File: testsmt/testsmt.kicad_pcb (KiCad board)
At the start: 2 copper layers, 100 x 100 mm, 47 parts, among them J1 DIN-5_180degree, J2 Conn_01x16, J3 Conn_01x16, J4 Conn_01x16, J5 AudioJack3_Ground_Switch, U1 6N138, U2 Teensy3.2, U3 4051, U4 4051, U5 4051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

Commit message: where is the last unrouted connection?!
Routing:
- net /DAC_OUTPUT: track 0.00 -> 99.1 mm, vias 0 -> 1
- net +5V: track 4.66 -> 94.6 mm, vias 0 -> 1
- net Net-(C2-Pad2): track 13.4 -> 96.1 mm, vias 0 -> 1
- net /KNOB_READ: track 0.00 -> 75.6 mm, vias 0 -> 1
- net +3V3: track 423.3 -> 477.0 mm, vias 5 -> 6
- net /LDR: track 0.00 -> 17.1 mm
- net GND: track 6.65 -> 18.6 mm, vias 4 -> 6
- net Net-(C2-Pad1): track 0.00 -> 11.5 mm
- net Net-(R1-Pad2): track 0.00 -> 9.89 mm
- net Net-(D1-Pad2): track 0.00 -> 3.12 mm
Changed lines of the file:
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@@
     (thickness 1.6)
     (drawings 15)
-    (tracks 815)
+    (tracks 886)
     (zones 0)
     (modules 47)
@@
   (segment (start 49.155 52.445) (end 49 52.6) (width 0.25) (layer F.Cu) (net 1))
   (via (at 50.3 39.9) (size 0.8) (drill 0.4) (layers F.Cu B.Cu) (net 1))
-  (via (at 139.1 32.284999) (size 0.8) (drill 0.4) (layers F.Cu B.Cu) (net 1))
   (segment (start 140.7 32.365) (end 139.180001 32.365) (width 0.25) (layer F.Cu) (net 1))
   (segment (start 139.180001 32.365) (end 139.1 32.284999) (width 0.25) (layer F.Cu) (net 1))
+  (via (at 139.1 32.284999) (size 0.8) (drill 0.4) (layers F.Cu B.Cu) (net 1))
+  (via (at 135.000011 38.4) (size 0.8) (drill 0.4) (layers F.Cu B.Cu) (net 1))
+  (segment (start 139.1 32.284999) (end 139.1 34.300011) (width 0.25) (layer B.Cu) (net 1))
+  (segment (start 139.1 34.300011) (end 135.000011 38.4) (width 0.25) (layer B.Cu) (net 1))
+  (segment (start 135.000011 37.744989) (end 135.3 37.445) (width 0.25) (layer F.Cu) (net 1))
+  (segment (start 135.000011 38.4) (end 135.000011 37.744989) (width 0.25) (layer F.Cu) (net 1))
+  (via (at 74.1 103.1) (size 0.8) (drill 0.4) (layers F.Cu B.Cu) (net 1))
+  (segment (start 74.1 102.925) (end 74.1 103.1) (width 0.25) (layer F.Cu) (net 1))
+  (segment (start 76.3 101.175) (end 75.85 101.175) (width 0.25) (layer F.Cu) (net 1))
+  (segment (start 75.85 101.175) (end 74.1 102.925) (width 0.25) (layer F.Cu) (net 1))
+  (via (at 94.6 98.7) (size 0.8) (drill 0.4) (layers F.Cu B.Cu) (net 3))
+  (segment (start 94.4 98.5) (end 94.6 98.7) (width 0.25) (layer F.Cu) (net 3))
+  (segment (start 125.08 62.51) (end 94.4 93.19) (width 0.25) (layer F.Cu) (net 3))
+  (segment (start 94.4 93.19) (end 94.4 98.5) (width 0.25) (layer F.Cu) (net 3))
+  (segment (start 50.899999 100.899999) (end 50 100) (width 0.25) (layer B.Cu) (net 3))
+  (segment (start 56.025001 106.025001) (end 50.899999 100.899999) (width 0.25) (layer B.Cu) (net 3))
+  (segment (start 87.274999 106.025001) (end 56.025001 106.025001) (width 0.25) (layer B.Cu) (net 3))
+  (segment (start 94.6 98.7) (end 87.274999 106.025001) (width 0.25) (layer B.Cu) (net 3))
   (via (at 46.3 60.3) (size 0.8) (drill 0.4) (layers F.Cu B.Cu) (net 5))
   (segment (start 46.3 71.730002) (end 46.3 60.3) (width 0.25) (layer F.Cu) (net 5))
@@
   (segment (start 117.46 63.64137) (end 108.54637 72.555) (width 0.25) (layer F.Cu) (net 5))
   (segment (start 117.46 62.51) (end 117.46 63.64137) (width 0.25) (layer F.Cu) (net 5))
-  (segment (start 56.7 72.555) (end 91 72.555) (width 0.25) (layer F.Cu) (net 5))
   (segment (start 91 72.555) (end 91.415 72.555) (width 0.25) (layer F.Cu) (net 5))
   (segment (start 117.46 61.37863) (end 117 60.91863) (width 0.25) (layer B.Cu) (net 5))
@@
   (segment (start 116.634315 26.8) (end 115.069316 28.364999) (width 0.25) (layer B.Cu) (net 5))
   (segment (start 117.2 26.8) (end 116.634315 26.8) (width 0.25) (layer B.Cu) (net 5))
+  (via (at 87.9 74.3) (size 0.8) (drill 0.4) (layers F.Cu B.Cu) (net 5))
+  (segment (start 80 84) (end 80 82.2) (width 0.25) (layer B.Cu) (net 5))
+  (segment (start 80 82.2) (end 87.9 74.3) (width 0.25) (layer B.Cu) (net 5))
+  (segment (start 89.645 72.555) (end 89.8 72.555) (width 0.25) (layer F.Cu) (net 5))
+  (segment (start 87.9 74.3) (end 89.645 72.555) (width 0.25) (layer F.Cu) (net 5))
+  (segment (start 56.7 72.555) (end 89.8 72.555) (width 0.25) (layer F.Cu) (net 5))
+  (segment (start 89.8 72.555) (end 91 72.555) (width 0.25) (layer F.Cu) (net 5))
+  (segment (start 106 119.727208) (end 106 121) (width 0.25) (layer F.Cu) (net 5))
+  (segment (start 106 116.822588) (end 106 119.727208) (width 0.25) (layer F.Cu) (net 5))
+  (segment (start 82.732412 93.555) (end 106 116.822588) (width 0.25) (layer F.Cu) (net 5))
+  (segment (start 81.7 93.555) (end 82.732412 93.555) (width 0.25) (layer F.Cu) (net 5))
   (segment (start 50.3 46.095) (end 47.2 49.195) (width 0.25) (layer F.Cu) (net 7))
   (segment (start 51.3 46.095) (end 50.3 46.095) (width 0.25) (layer F.Cu) (net 7))
@@
   (segment (start 51.5 70.3) (end 88.4 70.3) (width 0.25) (layer F.Cu) (net 7))
   (segment (start 88.4 70.3) (end 88.59 70.3) (width 0.25) (layer F.Cu) (net 7))
+  (segment (start 123.681237 67.443763) (end 123.125 68) (width 0.25) (layer F.Cu) (net 8))
+  (segment (start 126.494999 64.630001) (end 123.681237 67.443763) (width 0.25) (layer F.Cu) (net 8))
+  (segment (start 126.494999 61.095001) (end 126.494999 64.630001) (width 0.25) (layer F.Cu) (net 8))
+  (segment (start 127.62 59.97) (end 126.494999 61.095001) (width 0.25) (layer F.Cu) (net 8))
+  (via (at 79.3 94.1) (size 0.8) (drill 0.4) (layers F.Cu B.Cu) (net 10))
+  (segment (start 78.745 94.1) (end 79.3 94.1) (width 0.25) (layer F.Cu) (net 10))
+  (segment (start 76.3 96.095) (end 76.75 96.095) (width 0.25) (layer F.Cu) (net 10))
+  (segment (start 76.75 96.095) (end 78.745 94.1) (width 0.25) (layer F.Cu) (net 10))
+  (segment (start 97.695002 94.1) (end 129.8 61.995002) (width 0.25) (layer B.Cu) (net 10))
+  (segment (start 79.3 94.1) (end 97.695002 94.1) (width 0.25) (layer B.Cu) (net 10))
+  (segment (start 129.8 57.07) (end 127.62 54.89) (width 0.25) (layer B.Cu) (net 10))
+  (segment (start 129.8 61.995002) (end 129.8 57.07) (width 0.25) (layer B.Cu) (net 10))
   (segment (start 50.3 32.095) (end 50.224999 32.019999) (width 0.25) (layer F.Cu) (net 11))
   (segment (start 51.3 32.095) (end 50.3 32.095) (width 0.25) (layer F.Cu) (net 11))
@@
   (segment (start 122.1525 96.19) (end 122.3425 96) (width 0.25) (layer F.Cu) (net 20))
   (segment (start 117.765 96.19) (end 122.1525 96.19) (width 0.25) (layer F.Cu) (net 20))
+  (via (at 118.5 71.1) (size 0.8) (drill 0.4) (layers F.Cu B.Cu) (net 20))
+  (segment (start 126.494999 63.105001) (end 118.5 71.1) (width 0.25) (layer B.Cu) (net 20))
+  (segment (start 127.62 29.49) (end 126.494999 30.615001) (width 0.25) (layer B.Cu) (net 20))
+  (segment (start 126.494999 30.615001) (end 126.494999 63.105001) (width 0.25) (layer B.Cu) (net 20))
+  (segment (start 123.927609 71.1) (end 135 82.172391) (width 0.25) (layer F.Cu) (net 20))
+  (segment (start 118.5 71.1) (end 123.927609 71.1) (width 0.25) (layer F.Cu) (net 20))
+  (segment (start 122.898737 95.443763) (end 122.3425 96) (width 0.25) (layer F.Cu) (net 20))
+  (segment (start 123.36751 94.97499) (end 122.898737 95.443763) (width 0.25) (layer F.Cu) (net 20))
+  (segment (start 130.856419 94.97499) (end 123.36751 94.97499) (width 0.25) (layer F.Cu) (net 20))
+  (segment (start 135 90.831409) (end 130.856419 94.97499) (width 0.25) (layer F.Cu) (net 20))
+  (segment (start 135 82.172391) (end 135 90.831409) (width 0.25) (layer F.Cu) (net 20))
   (segment (start 52.3 75.095) (end 53.9 73.495) (width 0.25) (layer F.Cu) (net 26))
   (segment (start 51.3 75.095) (end 52.3 75.095) (width 0.25) (layer F.Cu) (net 26))
@@
   (segment (start 135.59 106) (end 135.51499 105.92499) (width 0.25) (layer F.Cu) (net 53))
   (segment (start 137.59 106) (end 135.59 106) (width 0.25) (layer F.Cu) (net 53))
+  (via (at 69.3 107.7) (size 0.8) (drill 0.4) (layers F.Cu B.Cu) (net 53))
+  (segment (start 64.00001 102.40001) (end 69.3 107.7) (width 0.25) (layer F.Cu) (net 53))
+  (segment (start 63 97.3) (end 64.00001 98.30001) (width 0.25) (layer F.Cu) (net 53))
+  (segment (start 64.00001 98.30001) (end 64.00001 102.40001) (width 0.25) (layer F.Cu) (net 53))
+  (segment (start 137.59 107.125) (end 137.59 106) (width 0.25) (layer B.Cu) (net 53))
+  (segment (start 137.015 107.7) (end 137.59 107.125) (width 0.25) (layer B.Cu) (net 53))
+  (segment (start 69.3 107.7) (end 137.015 107.7) (width 0.25) (layer B.Cu) (net 53))
   (segment (start 129.5009 88.99618) (end 120.50382 88.99618) (width 0.25) (layer F.Cu) (net 54))
   (segment (start 120.50382 88.99618) (end 112.5 97) (width 0.25) (layer F.Cu) (net 54))
@@
   (segment (start 121.87118 79.00382) (end 129.5009 79.00382) (width 0.25) (layer F.Cu) (net 57))
   (segment (start 104.875 96) (end 121.87118 79.00382) (width 0.25) (layer F.Cu) (net 57))
+  (segment (start 125.5875 68) (end 128.125 68) (width 0.25) (layer F.Cu) (net 59))
+  (segment (start 125 68) (end 125.5875 68) (width 0.25) (layer F.Cu) (net 59))
+  (segment (start 75.85 94.825) (end 76.3 94.825) (width 0.25) (layer F.Cu) (net 60))
+  (segment (start 75.224999 94.199999) (end 75.85 94.825) (width 0.25) (layer F.Cu) (net 60))
+  (segment (start 75.224999 87.437082) (end 75.224999 94.199999) (width 0.25) (layer F.Cu) (net 60))
+  (segment (start 77.46 85.202081) (end 75.224999 87.437082) (width 0.25) (layer F.Cu) (net 60))
+  (segment (start 77.46 84) (end 77.46 85.202081) (width 0.25) (layer F.Cu) (net 60))
+  (segment (start 72.7625 94.825) (end 72 94.0625) (width 0.25) (layer F.Cu) (net 60))
+  (segment (start 76.3 94.825) (end 72.7625 94.825) (width 0.25) (layer F.Cu) (net 60))
   (segment (start 136.745 70.4775) (end 139.3625 70.4775) (width 0.25) (layer F.Cu) (net 61))
   (segment (start 136.1575 70.4775) (end 136.745 70.4775) (width 0.25) (layer F.Cu) (net 61))
@@
   (segment (start 135.1 65.58) (end 134.2825 66.3975) (width 0.25) (layer F.Cu) (net 78))
   (segment (start 135.1 65) (end 135.1 65.58) (width 0.25) (layer F.Cu) (net 78))
+  (segment (start 53.399999 100.899999) (end 52.5 100) (width 0.25) (layer F.Cu) (net 79))
+  (segment (start 53.725001 101.225001) (end 53.399999 100.899999) (width 0.25) (layer F.Cu) (net 79))
+  (segment (start 60.999999 101.225001) (end 53.725001 101.225001) (width 0.25) (layer F.Cu) (net 79))
+  (segment (start 62.225 100) (end 60.999999 101.225001) (width 0.25) (layer F.Cu) (net 79))
+  (segment (start 63 100) (end 62.225 100) (width 0.25) (layer F.Cu) (net 79))
   (segment (start 82.15 97.365) (end 81.7 97.365) (width 0.25) (layer F.Cu) (net 80))
   (segment (start 83.95001 99.16501) (end 82.15 97.365) (width 0.25) (layer F.Cu) (net 80))

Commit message: routing done
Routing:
- net Net-(U2-Pad52): track 0.00 -> 3.81 mm
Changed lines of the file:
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@@
     (thickness 1.6)
     (drawings 15)
-    (tracks 886)
+    (tracks 888)
     (zones 0)
     (modules 47)
@@
     (38 B.Mask user)
     (39 F.Mask user)
-    (40 Dwgs.User user hide)
+    (40 Dwgs.User user)
     (41 Cmts.User user)
     (42 Eco1.User user)
@@
   (segment (start 124.1 98.9) (end 122 101) (width 0.25) (layer F.Cu) (net 36))
   (segment (start 124.9 98.9) (end 124.1 98.9) (width 0.25) (layer F.Cu) (net 36))
+  (segment (start 120 38.306498) (end 120 35.84) (width 0.25) (layer F.Cu) (net 50))
+  (segment (start 120 39.65) (end 120 38.306498) (width 0.25) (layer F.Cu) (net 50))
   (segment (start 136.715 96) (end 137.59 96) (width 0.25) (layer F.Cu) (net 53))
   (segment (start 135.51499 97.20001) (end 136.715 96) (width 0.25) (layer F.Cu) (net 53))

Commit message: nearly there
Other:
- board text added: "Attack"
- board text added: "Cutoff"
- board text added: "DAC volume"
- board text added: "Decay"
- board text added: "LFO (out) Saw (out) Square (out) Filter (out) ADSR (out) VCA (out) MIDI note (out) MIDI gate (out) Saw freq (in) Square freq (in) Filter (in) Filter cutoff (in) VCA (in) VCA CV (in) ADSR gate (in) Main out (in)"
- board text added: "LFO freq"
- board text added: "Release"
- board text added: "Resonance"
- board text added: "Saw freq"
- board text added: "Sustain"
- board text added: "by Matt Bradshaw"
- board text added: "polymod mini v1"
- board text removed: "Parameter X Parameter X Parameter X Parameter X Parameter X Parameter X Parameter X Parameter X Parameter X Parameter X Parameter X Parameter X Parameter X Parameter X Parameter X Parameter X"
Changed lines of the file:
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@@
   (general
     (thickness 1.6)
-    (drawings 15)
+    (drawings 26)
     (tracks 888)
     (zones 0)
@@
       (net 50 "Net-(U2-Pad52)"))
   )
+  (gr_text "by Matt\nBradshaw" (at 59.5 85) (layer F.SilkS)
+    (effects (font (size 1.5 1.5) (thickness 0.3)) (justify left))
+  )
+  (gr_text "polymod mini v1" (at 59 79.5) (layer F.SilkS)
+    (effects (font (size 2.5 2.5) (thickness 0.5)) (justify left))
+  )
+  (gr_text "LFO freq" (at 78.5 88) (layer F.SilkS)
+    (effects (font (size 1.5 1.5) (thickness 0.3)))
+  )
+  (gr_text Cutoff (at 104 93) (layer F.SilkS)
+    (effects (font (size 1.5 1.5) (thickness 0.3)))
+  )
+  (gr_text Release (at 137.5 123) (layer F.SilkS)
+    (effects (font (size 1.5 1.5) (thickness 0.3)))
+  )
+  (gr_text Sustain (at 120.5 123) (layer F.SilkS)
+    (effects (font (size 1.5 1.5) (thickness 0.3)))
+  )
+  (gr_text Decay (at 103.5 123) (layer F.SilkS)
+    (effects (font (size 1.5 1.5) (thickness 0.3)))
+  )
+  (gr_text Attack (at 86.5 123) (layer F.SilkS)
+    (effects (font (size 1.5 1.5) (thickness 0.3)))
+  )
+  (gr_text Resonance (at 69.5 123) (layer F.SilkS)
+    (effects (font (size 1.5 1.5) (thickness 0.3)))
+  )
+  (gr_text "Saw freq" (at 52.7 123) (layer F.SilkS)
+    (effects (font (size 1.5 1.5) (thickness 0.3)))
+  )
+  (gr_text "DAC volume" (at 52.7 102.6) (layer F.SilkS)
+    (effects (font (size 1.5 1.5) (thickness 0.3)))
+  )
   (gr_line (start 99 50) (end 99 92) (layer Dwgs.User) (width 0.2))
   (gr_line (start 109 50) (end 99 50) (layer Dwgs.User) (width 0.2))
@@
   (gr_line (start 145 25) (end 145 125) (layer Edge.Cuts) (width 0.2))
   (gr_line (start 45 25) (end 145 25) (layer Edge.Cuts) (width 0.2))
-  (gr_text "Parameter X\nParameter X\nParameter X\nParameter X\nParameter X\nParameter X\nParameter X\nParameter X\nParameter X\nParameter X\nParameter X\nParameter X\nParameter X\nParameter X\nParameter X\nParameter X" (at 85.6 48) (layer F.SilkS)
-    (effects (font (size 1.5 1.5) (thickness 0.3)))
+  (gr_text "LFO (out)\nSaw (out)\nSquare (out)\nFilter (out)\nADSR (out)\nVCA (out)\nMIDI note (out)\nMIDI gate (out)\nSaw freq (in)\nSquare freq (in)\nFilter (in)\nFilter cutoff (in)\nVCA (in)\nVCA CV (in)\nADSR gate (in)\nMain out (in)" (at 78.7 48) (layer F.SilkS)
+    (effects (font (size 1.5 1.5) (thickness 0.3)) (justify left))
   )
   (via (at 49.2 65.1) (size 0.8) (drill 0.4) (layers F.Cu B.Cu) (net 1))

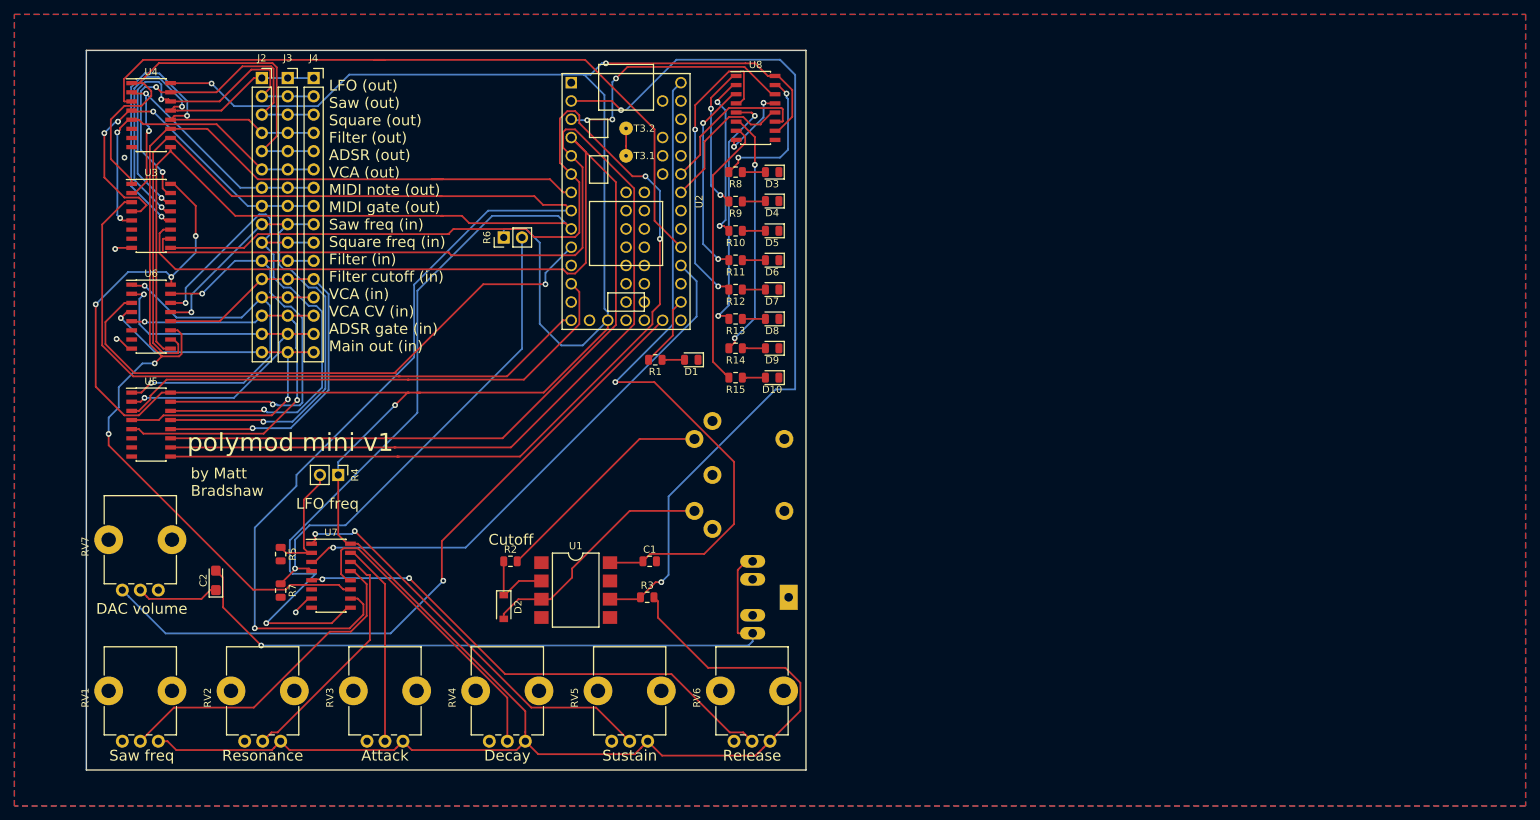
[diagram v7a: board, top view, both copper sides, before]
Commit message: mounting holes
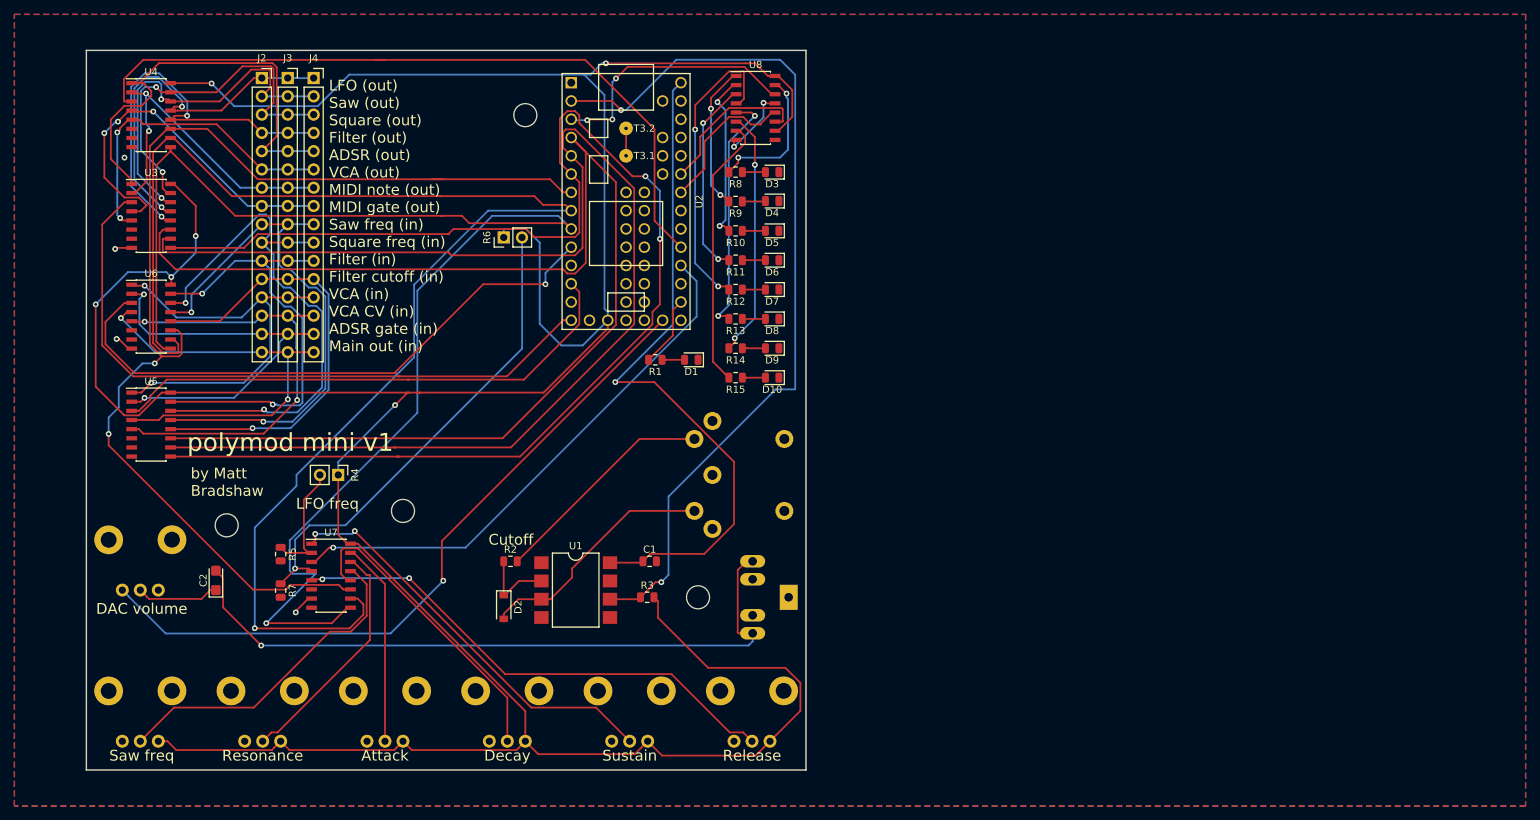
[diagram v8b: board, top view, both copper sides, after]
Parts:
- added H1: MountingHole, polymodsmt:MountingHole_3.2mm_M3, F.Cu at (64.5, 91.0)
- added H2: MountingHole, polymodsmt:MountingHole_3.2mm_M3, F.Cu at (106.0, 34.0)
- added H3: MountingHole, polymodsmt:MountingHole_3.2mm_M3, F.Cu at (130.0, 101.0)
- added H4: MountingHole, polymodsmt:MountingHole_3.2mm_M3, F.Cu at (89.0, 89.0)
- RV1, RV2, RV3, RV4, RV5, RV6, RV7: footprint Potentiometer_THT:Potentiometer_Alps_RK09K_Single_Vertical -> polymodsmt:Potentiometer_Alps_RK09K_Single_Vertical
